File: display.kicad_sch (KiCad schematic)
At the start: 21 parts, among them Q1 HL2300, Q2 HL2300, Q3 HL2300, Q4 HL2300, Q5 HL2300, Q6 HL2300, Q7 HL2300, Q8 HL2300, U5 GS3911AG

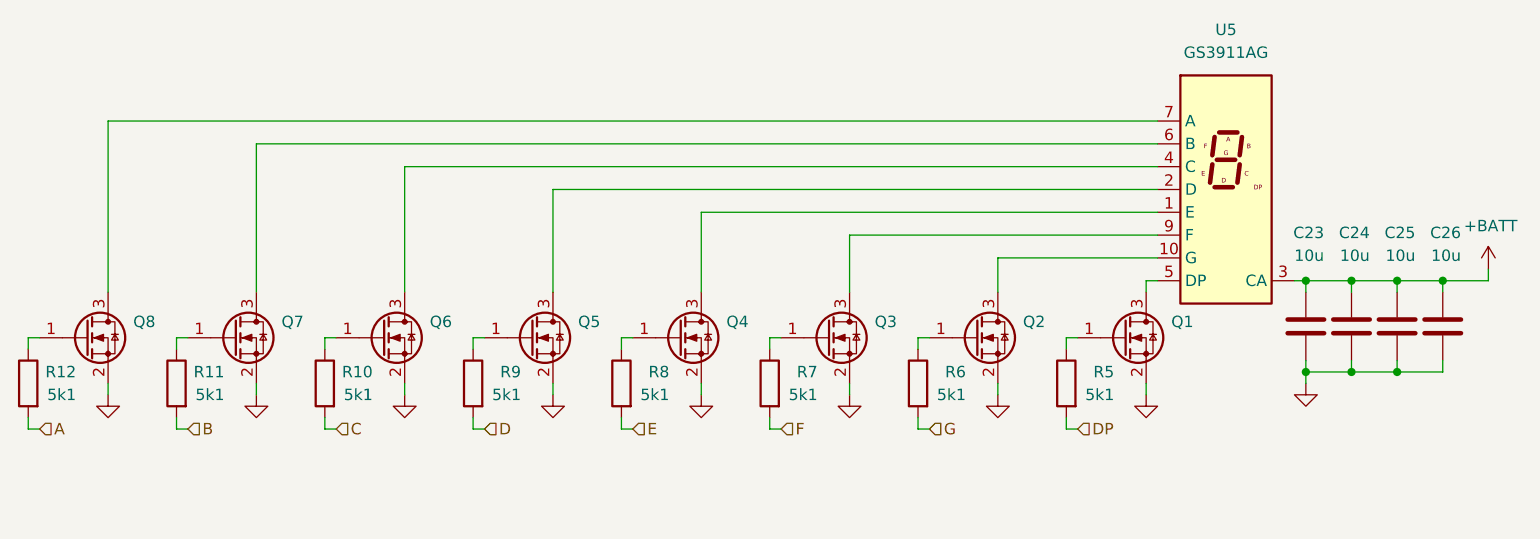
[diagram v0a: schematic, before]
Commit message: schem: add segment display series resistors
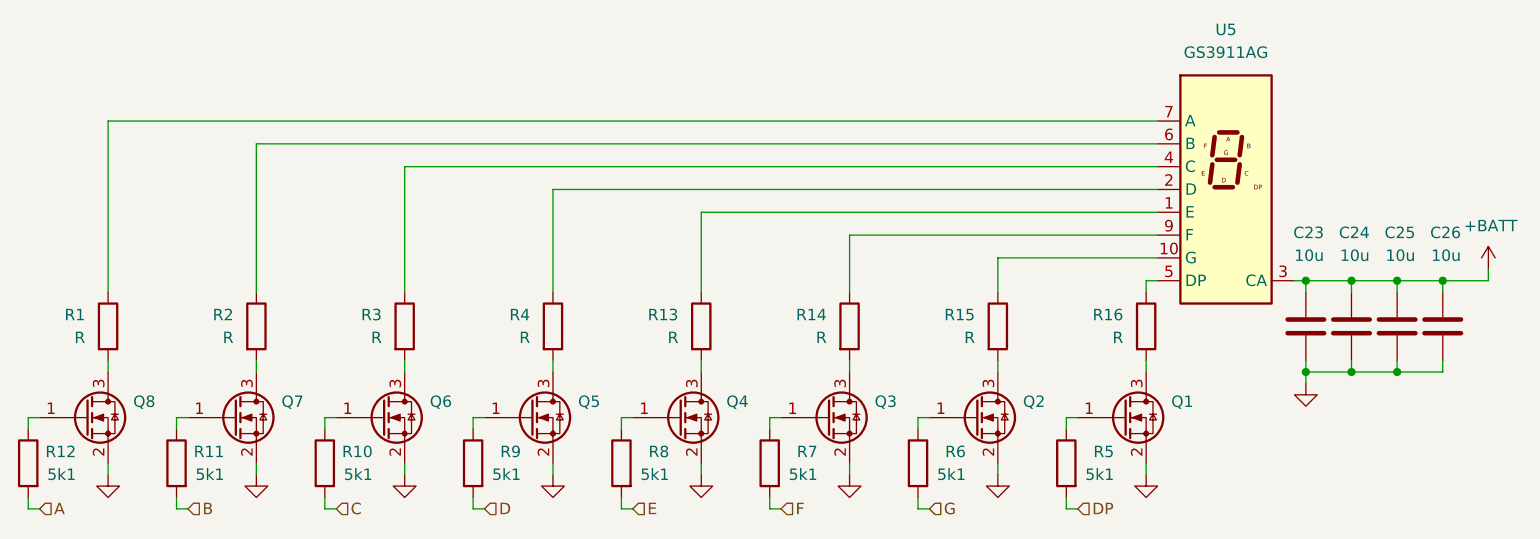
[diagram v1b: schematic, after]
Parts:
- added R1, R13, R14, R15, R16, R2, R3, R4: R, symbol Device:R
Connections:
- net at Q8.3 (D): now also R1.2; no longer U5.7 (A)
- net at U5.4 (C): now also R3.1; no longer Q6.3 (D)
- net at Q3.3 (D): now also R14.2; no longer U5.9 (F)
- net at U5.5 (DP): now also R16.1; no longer Q1.3 (D)
- net at U5.1 (E): now also R13.1; no longer Q4.3 (D)
- net at U5.10 (G): now also R15.1; no longer Q2.3 (D)
- net at U5.2 (D): now also R4.1; no longer Q5.3 (D)
- net at U5.6 (B): now also R2.1; no longer Q7.3 (D)
- new net: Q4.3 (D), R13.2
- new net: Q1.3 (D), R16.2
- new net: Q5.3 (D), R4.2
- new net: Q6.3 (D), R3.2
- new net: Q2.3 (D), R15.2
- new net: R1.1, U5.7 (A)
- new net: R14.1, U5.9 (F)
- new net: Q7.3 (D), R2.2
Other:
- moved on the sheet: Q1, Q2, Q3, Q4, Q5, Q6, Q7, Q8, R10, R11, R12, R5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

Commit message: schem: add led series resistors pns
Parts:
- R1, R13, R14, R15, R16, R2, R3, R4: value R -> 470; footprint (none) -> Resistor_SMD:R_0402_1005Metric; Basic (none) -> Y; JLCPCB Part # (none) -> C25117; Manufacturer (none) -> Uniroyal Elec; Manufacturer Part Number (none) -> 0402WGF4700TCE

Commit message: schem: add ordering info to BOM
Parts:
- Q1, Q2, Q3, Q4, Q5, Q6, Q7, Q8: Basic (none) -> E; JLCPCB Part # (none) -> C7420343; Manufacturer (none) -> hongjiacheng; Manufacturer Part Number (none) -> HL2300
- U5: Basic (none) -> X; JLCPCB Part # (none) -> C22462667; Manufacturer (none) -> Guangcai Display; Manufacturer Part Number (none) -> GS3911AG-G

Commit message: schem: add title
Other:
- company: (none) -> Rémi Ait-Younes
- title: (none) -> DYB Segment Driver 1
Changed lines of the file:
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@@
 	(generator_version "10.0")
 	(paper "A4")
+	(title_block
+		(title "DYB Segment Driver 1")
+		(date "2026-09-29")
+		(rev "01")
+		(company "Rémi Ait-Younes")
+	)
 	(junction
 		(at 231.14 88.9)

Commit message: schem: reannotate
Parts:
- renumbered C23 to C3, C24 to C4, C25 to C5, C26 to C6, Q8 to Q1, Q7 to Q2, Q6 to Q3, Q5 to Q4, Q4 to Q5, Q3 to Q6, Q2 to Q7, Q1 to Q8, R12 to R1, R13 to R10, R7 to R11, R14 to R12, R6 to R13, R15 to R14, R5 to R15, R1 to R2, R11 to R3, R2 to R4, R10 to R5, R3 to R6, R9 to R7, R4 to R8, R8 to R9, U5 to U2

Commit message: schem: fix footprints
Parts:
- U2: footprint Package_TO_SOT_SMD:SOT-23 -> (none)
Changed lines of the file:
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@@
 			)
 		)
-		(property "Footprint" "Package_TO_SOT_SMD:SOT-23"
+		(property "Footprint" ""
 			(at 207.01 93.98 0)
 			(hide yes)

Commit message: schem: add segment display footprint
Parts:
- U2: footprint (none) -> GLCS:GS3911AG
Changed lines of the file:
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@@
 			)
 		)
-		(property "Footprint" ""
+		(property "Footprint" "GLCS:GS3911AG"
 			(at 207.01 93.98 0)
 			(hide yes)
